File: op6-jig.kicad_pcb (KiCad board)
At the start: 4 copper layers, 75 x 60.6 mm, 43 parts, among them J1 PHONE_TP_BREAKOUT, J2 JTAG_ATMEGA, J4 TYPE-C-31-M-12, J5 TYPE-C-31-M-12, SW1 SW_RESET, U1 ATMEGA32U4, U2 LSF0102YZTR, U3 AP2192, Y1 16MHz

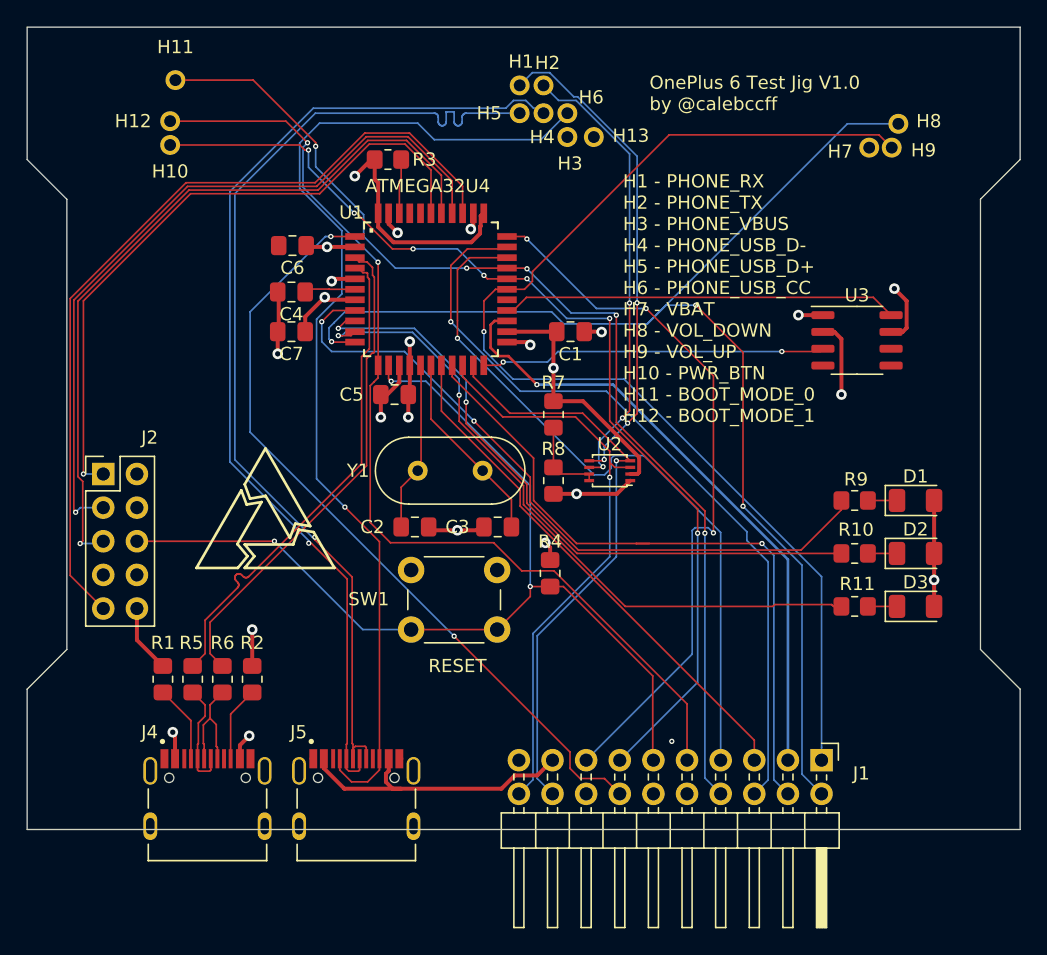
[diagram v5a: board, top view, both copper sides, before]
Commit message: Final-final-v2.docx (it's ordered)
- Replaced the precisely positioned and probably wrong test points with
  a pin header connector which can just be soldered too.
- Cleaned up some traces, resized all vias to be a minimum of 0.45mm for
  JLCPCB.
- Ordered the board!
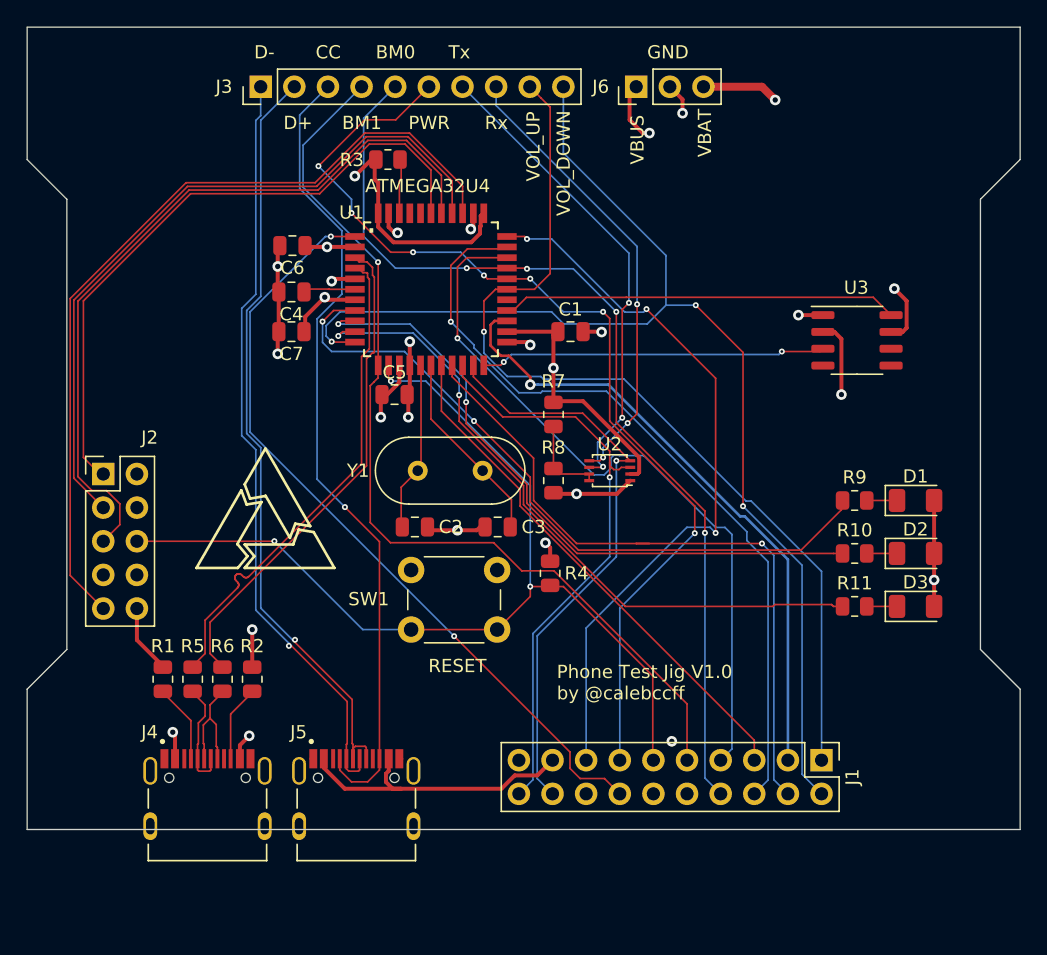
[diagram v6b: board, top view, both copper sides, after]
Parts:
- removed H1: Rx, op6-jig:TestPoint_Plated_Hole_D0.9mm
- removed H10: PWR_BTN, op6-jig:TestPoint_Plated_Hole_D0.9mm
- removed H11: BOOT_MODE_0, op6-jig:TestPoint_Plated_Hole_D0.9mm
- removed H12: BOOT_MODE_1, op6-jig:TestPoint_Plated_Hole_D0.9mm
- removed H13: GND, op6-jig:TestPoint_Plated_Hole_D0.9mm
- removed H2: Tx, op6-jig:TestPoint_Plated_Hole_D0.9mm
- removed H3: PHONE_VBUS, op6-jig:TestPoint_Plated_Hole_D0.9mm
- removed H4: PHONE_USB_D-, op6-jig:TestPoint_Plated_Hole_D0.9mm
- removed H5: PHONE_USB_D+, op6-jig:TestPoint_Plated_Hole_D0.9mm
- removed H6: PHONE_USB_CC, op6-jig:TestPoint_Plated_Hole_D0.9mm
- removed H7: VBAT0, op6-jig:TestPoint_Plated_Hole_D0.9mm
- removed H8: VOL_DOWN, op6-jig:TestPoint_Plated_Hole_D0.9mm
- removed H9: VOL_UP, op6-jig:TestPoint_Plated_Hole_D0.9mm
- added J3: CONN_PHONE_DATA, Connector_PinHeader_2.54mm:PinHeader_1x10_P2.54mm_Vertical, F.Cu at (89.6, 75.5)
- added J6: CONN_PHONE_POWER, Connector_PinHeader_2.54mm:PinHeader_1x03_P2.54mm_Vertical, F.Cu at (118.0, 75.5)
- C1, C2, C3, C4, C5, C6, C7: footprint Capacitor_SMD:C_0805_2012Metric_Pad1.18x1.45mm_HandSolder -> Capacitor_SMD:C_0805_2012Metric
- J1: footprint Connector_PinHeader_2.54mm:PinHeader_2x10_P2.54mm_Horizontal -> Connector_PinHeader_2.54mm:PinHeader_2x10_P2.54mm_Vertical
- R1, R10, R11, R2, R3, R4, R5, R6, R7, R8, R9: footprint Resistor_SMD:R_0805_2012Metric_Pad1.20x1.40mm_HandSolder -> Resistor_SMD:R_0805_2012Metric
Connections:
- J1 pad 12: (no net) -> Net-(J1-Pad12)
- J1 pad 16: (no net) -> Net-(J1-Pad16)
- J2 pad 7: (no net) -> Net-(J2-Pad7)
- J2 pad 8: (no net) -> Net-(J2-Pad8)
- J4 pad A8: (no net) -> Net-(J4-PadA8)
- J4 pad B8: (no net) -> Net-(J4-PadB8)
- J5 pad A8: (no net) -> Net-(J5-PadA8)
- J5 pad B8: (no net) -> Net-(J5-PadB8)
- U1 pad 27: (no net) -> Net-(U1-Pad27)
- U1 pad 40: (no net) -> Net-(U1-Pad40)
- U1 pad 41: (no net) -> Net-(U1-Pad41)
- U3 pad 4: (no net) -> Net-(U3-Pad4)
- U3 pad 5: (no net) -> Net-(U3-Pad5)
- U3 pad 6: (no net) -> Net-(U3-Pad6)
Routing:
- net PHONE_USB_D-: track 76.3 -> 57.5 mm
- net PHONE_USB_D+: track 76.4 -> 58.4 mm
- net PHONE_USB_CC: track 78.2 -> 61.1 mm
- net VOL_UP: track 87.0 -> 71.1 mm
- net VBAT: track 99.6 -> 112.2 mm, vias 1 -> 2
- net BOOT_MODE_0: track 82.1 -> 73.4 mm, vias 5 -> 4
- net GND: track 49.4 -> 55.7 mm, vias 13 -> 15
- net BOOT_MODE_1: track 76.3 -> 71.2 mm, vias 2 -> 1
- net VOL_DOWN: track 98.1 -> 93.0 mm
- net PHONE_RX: track 37.0 -> 34.6 mm
- net JTAG_TCO: track 55.8 -> 54.1 mm, vias 1 -> 0
- net PHONE_TX: track 34.4 -> 36.1 mm
- net PHONE_VBUS_SWITCHED: track 34.1 -> 32.6 mm, vias 1 -> 2
- net PWR_BTN: track 78.0 -> 76.6 mm
- net ATMEGA_PC6: track 54.1 -> 55.4 mm
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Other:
- net class Default: via_dia 0.8 -> 0.45; via_drill 0.4 -> 0.2
- rule via_min_size: 0.4 -> 0.45
- board text added: "BM0"
- board text added: "BM1"
- board text added: "CC"
- board text added: "D+"
- board text added: "D-"
- board text added: "GND"
- board text added: "JLCJLCJLCJLC"
- board text added: "PWR"
- board text added: "Phone Test Jig V1.0 by @calebccff"
- board text added: "Rx"
- board text added: "Tx"
- board text added: "VBAT"
- board text added: "VBUS"
- board text added: "VOL_DOWN"
- board text added: "VOL_UP"
- board text removed: "H1 - PHONE_RX H2 - PHONE_TX H3 - PHONE_VBUS H4 - PHONE_USB_D- H5 - PHONE_USB_D+ H6 - PHONE_USB_CC H7 - VBAT H8 - VOL_DOWN H9 - VOL_UP H10 - PWR_BTN H11 - BOOT_MODE_0 H12 - BOOT_MODE_1"
- board text removed: "OnePlus 6 Test Jig V1.0 by @calebccff"

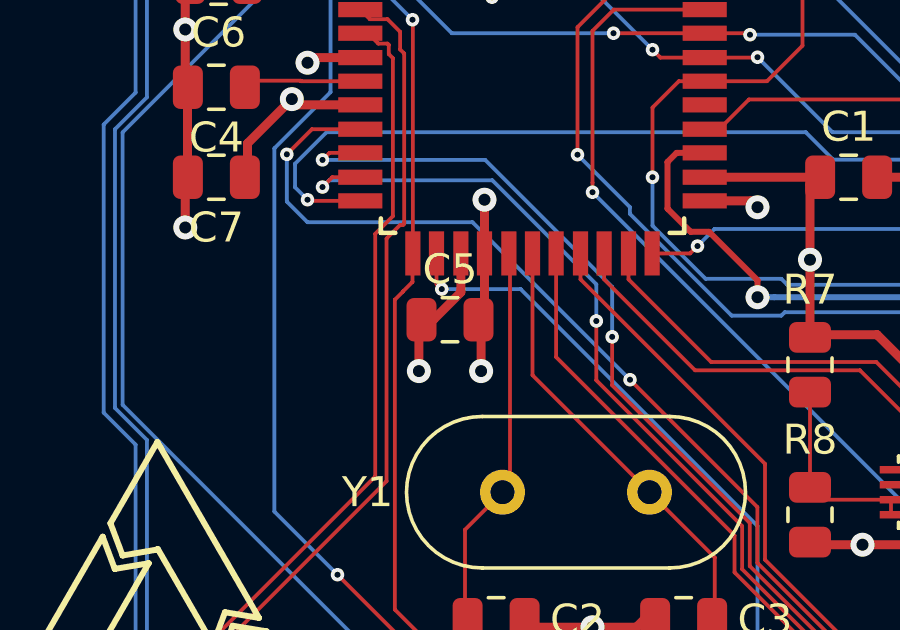
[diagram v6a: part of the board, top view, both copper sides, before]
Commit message: fix some cap spacing
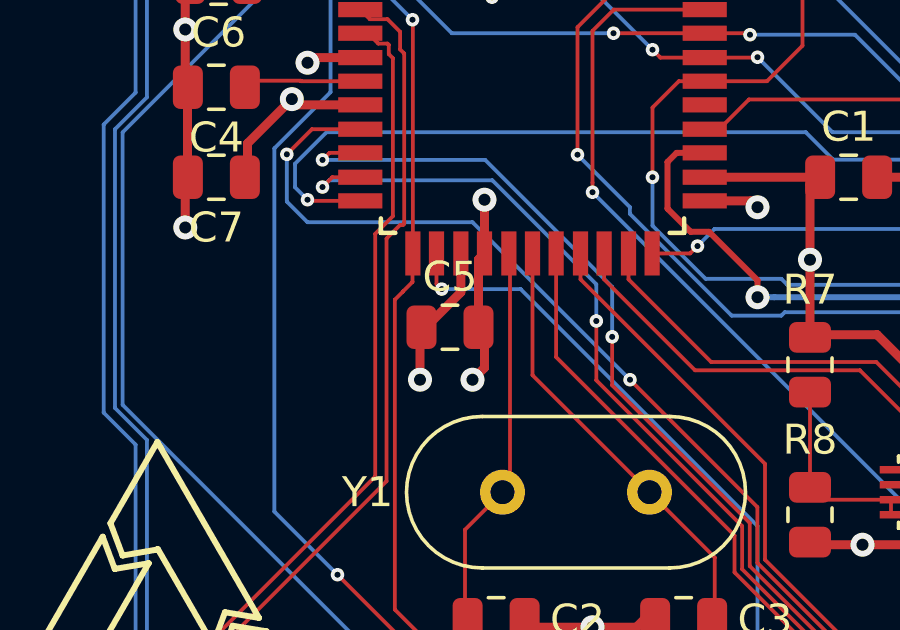
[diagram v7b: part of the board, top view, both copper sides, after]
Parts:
- moved C5 0.25 mm to (99.8, 99.0)
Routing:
- net GND: track 55.7 -> 56.2 mm
